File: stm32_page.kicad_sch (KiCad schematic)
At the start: 20 parts, among them J1 FTSH-107-01-L-DV-K-A, U1 STM32L431KBU6_C2826408, X1 SC-32S32.768kHz20PPM7pF

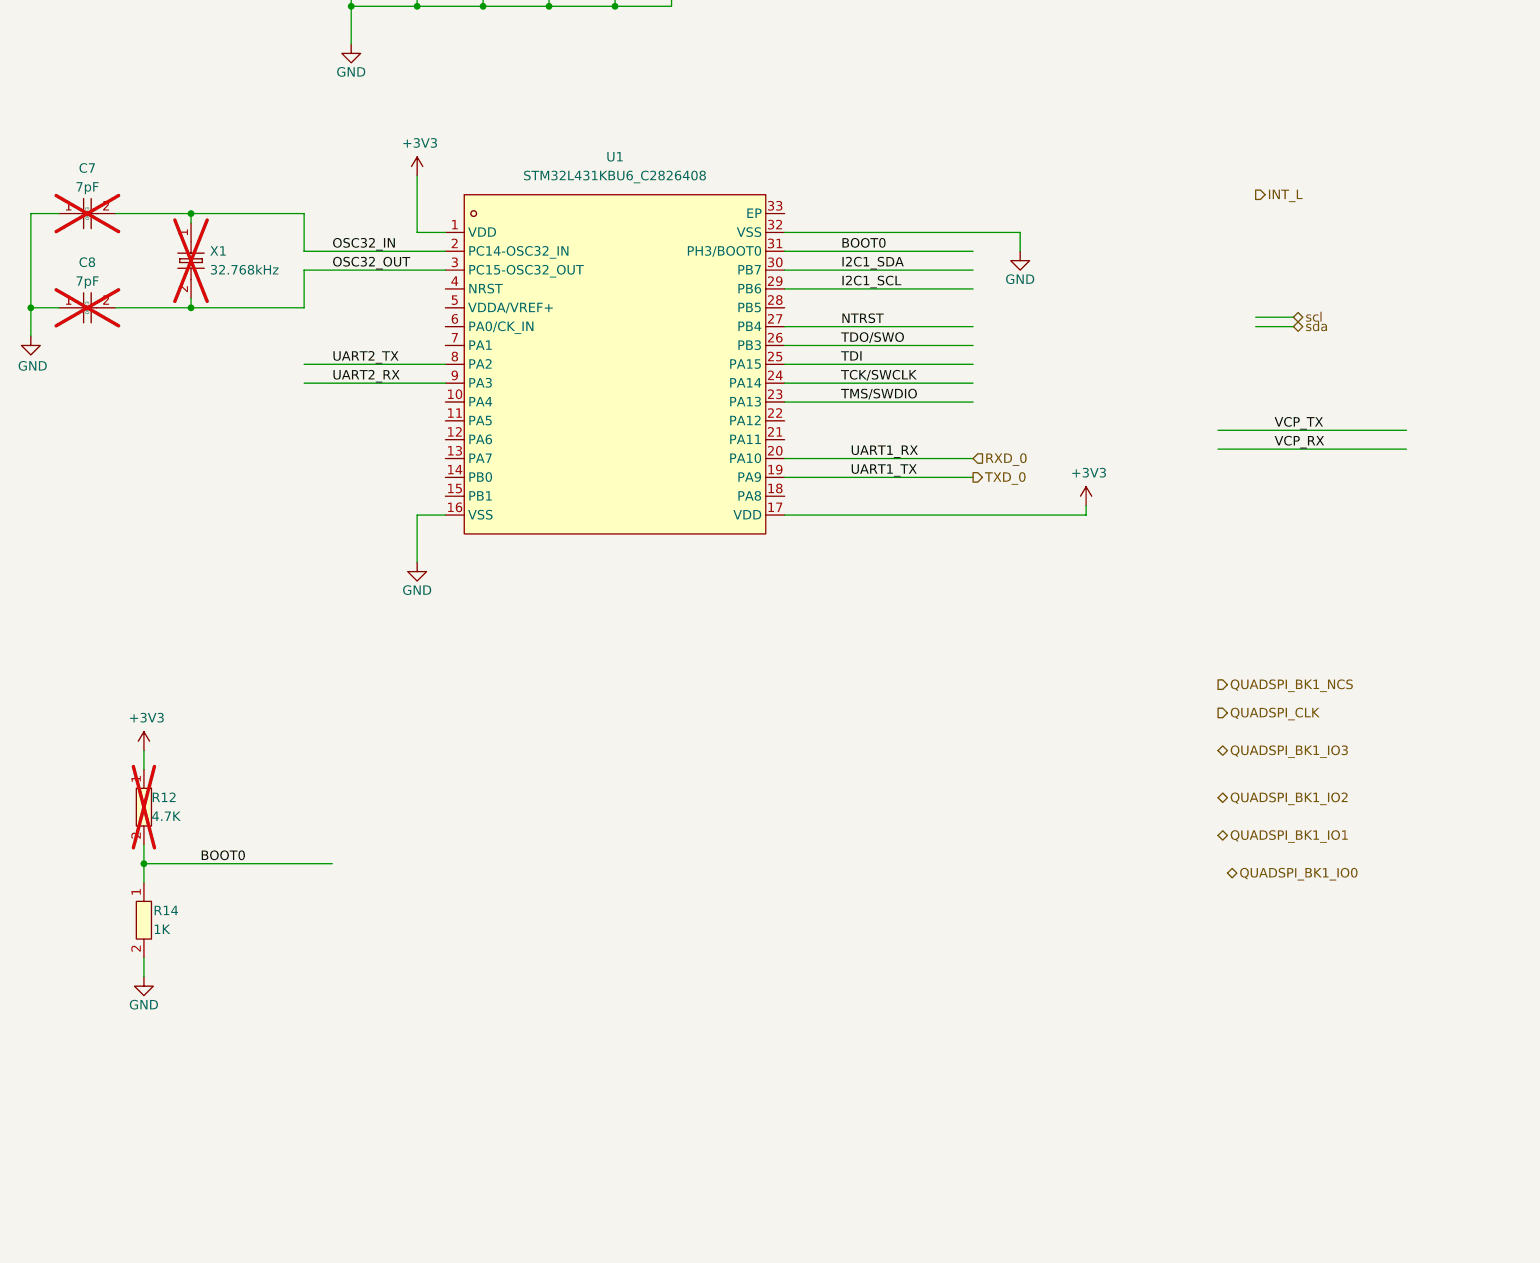
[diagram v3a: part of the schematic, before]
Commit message: Add IO pinout - 2 I2C, 2UART, 1 SPI, LEDs, switches,2 interupts,RST
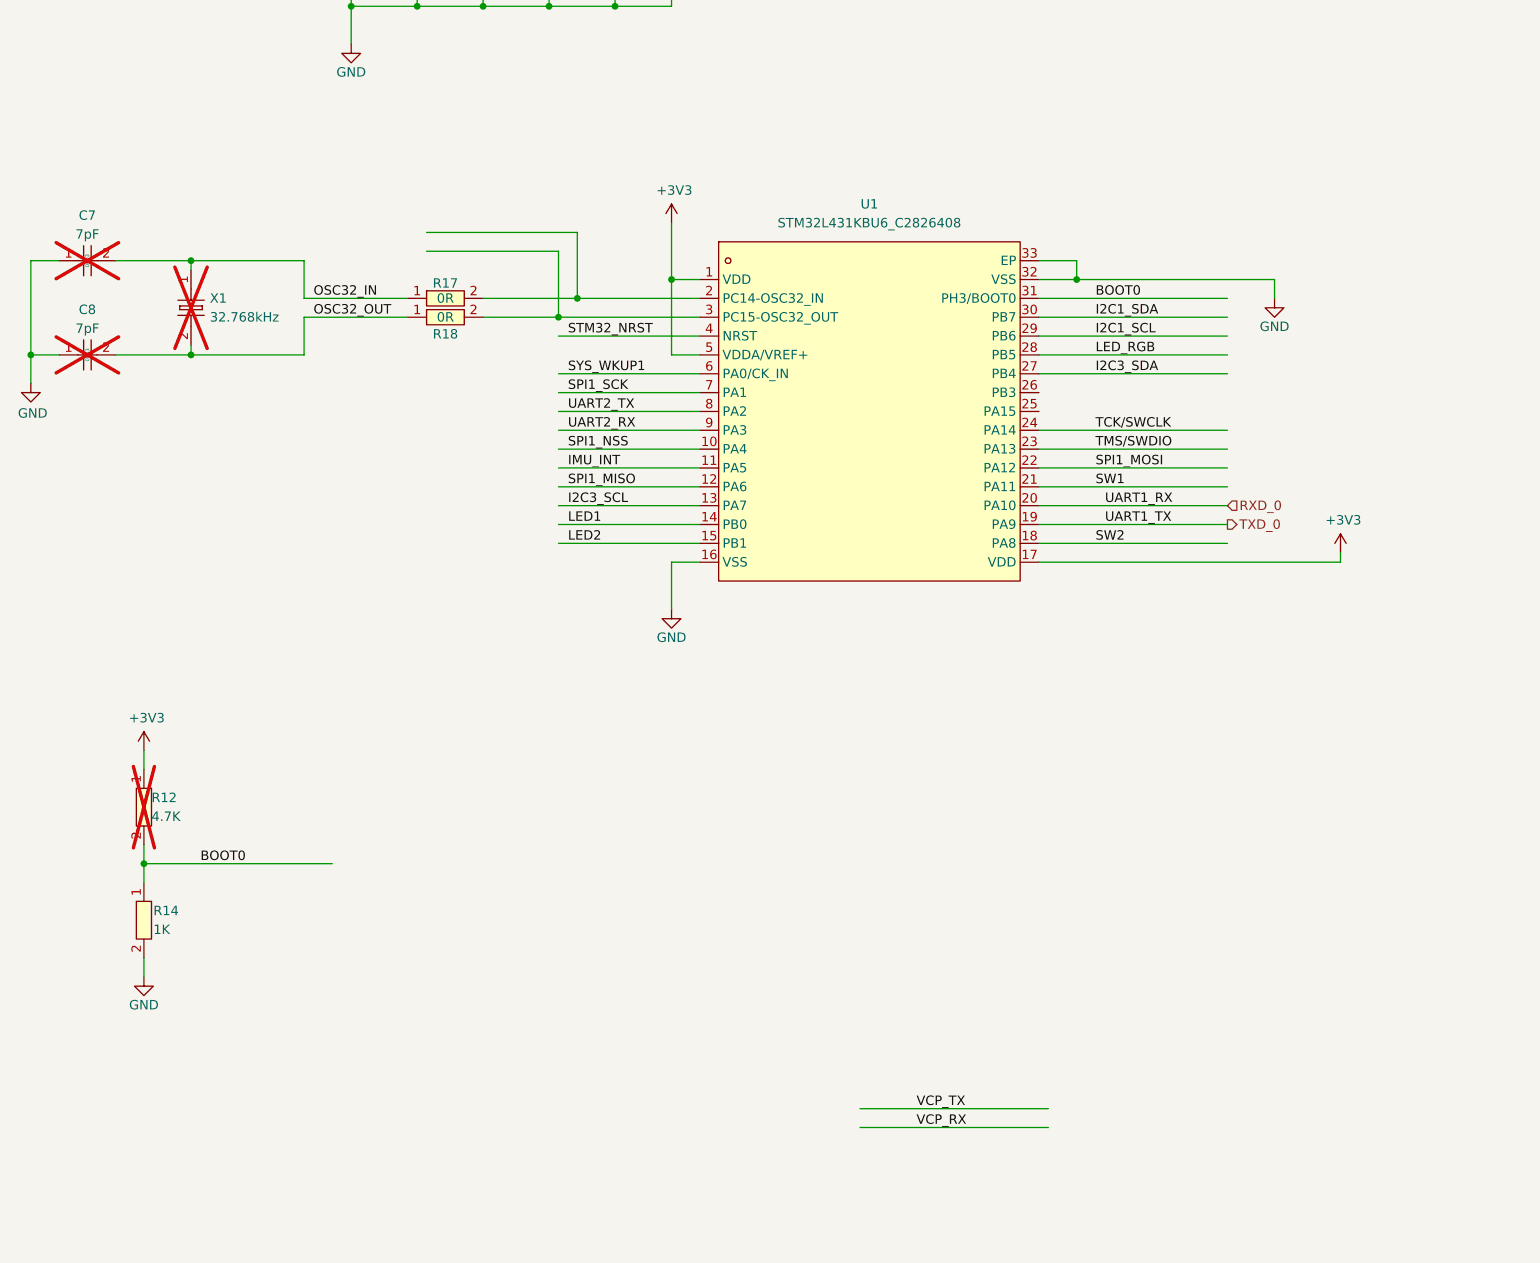
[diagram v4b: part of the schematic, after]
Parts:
- added R17, R18: 0603WAF0000T5E, easyeda2kicad:R0603, symbol easyeda2kicad:0603WAF0000T5E
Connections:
- net +3V3: now also U1.5 (VDDA/VREF+)
- net GND: now also U1.33 (EP)
- net NTRST: no longer U1.27 (PB4)
- net OSC32_IN: now also R17.1; no longer U1.2 (PC14-OSC32_IN)
- net OSC32_OUT: now also R18.1; no longer U1.3 (PC15-OSC32_OUT)
- net TDI: no longer U1.25 (PA15)
- net TDO/SWO: no longer U1.26 (PB3)
- net SPI1_NSS: now reaches U1.10 (PA4)
- net IMU_INT: now reaches U1.11 (PA5)
- net SPI1_MISO: now reaches U1.12 (PA6)
- net I2C3_SCL: now reaches U1.13 (PA7)
- net LED1: now reaches U1.14 (PB0)
- net LED2: now reaches U1.15 (PB1)
- net SW2: now reaches U1.18 (PA8)
- net SW1: now reaches U1.21 (PA11)
- net SPI1_MOSI: now reaches U1.22 (PA12)
- net LED_RGB: now reaches U1.28 (PB5)
- net STM32_NRST: now reaches U1.4 (NRST)
- net SYS_WKUP1: now reaches U1.6 (PA0/CK_IN)
- net SPI1_SCK: now reaches U1.7 (PA1)
- new net: R17.2, U1.2 (PC14-OSC32_IN)
- new net: R18.2, U1.3 (PC15-OSC32_OUT)
- new net I2C3_SDA: U1.27 (PB4)
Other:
- moved on the sheet: C7, C8, U1, X1

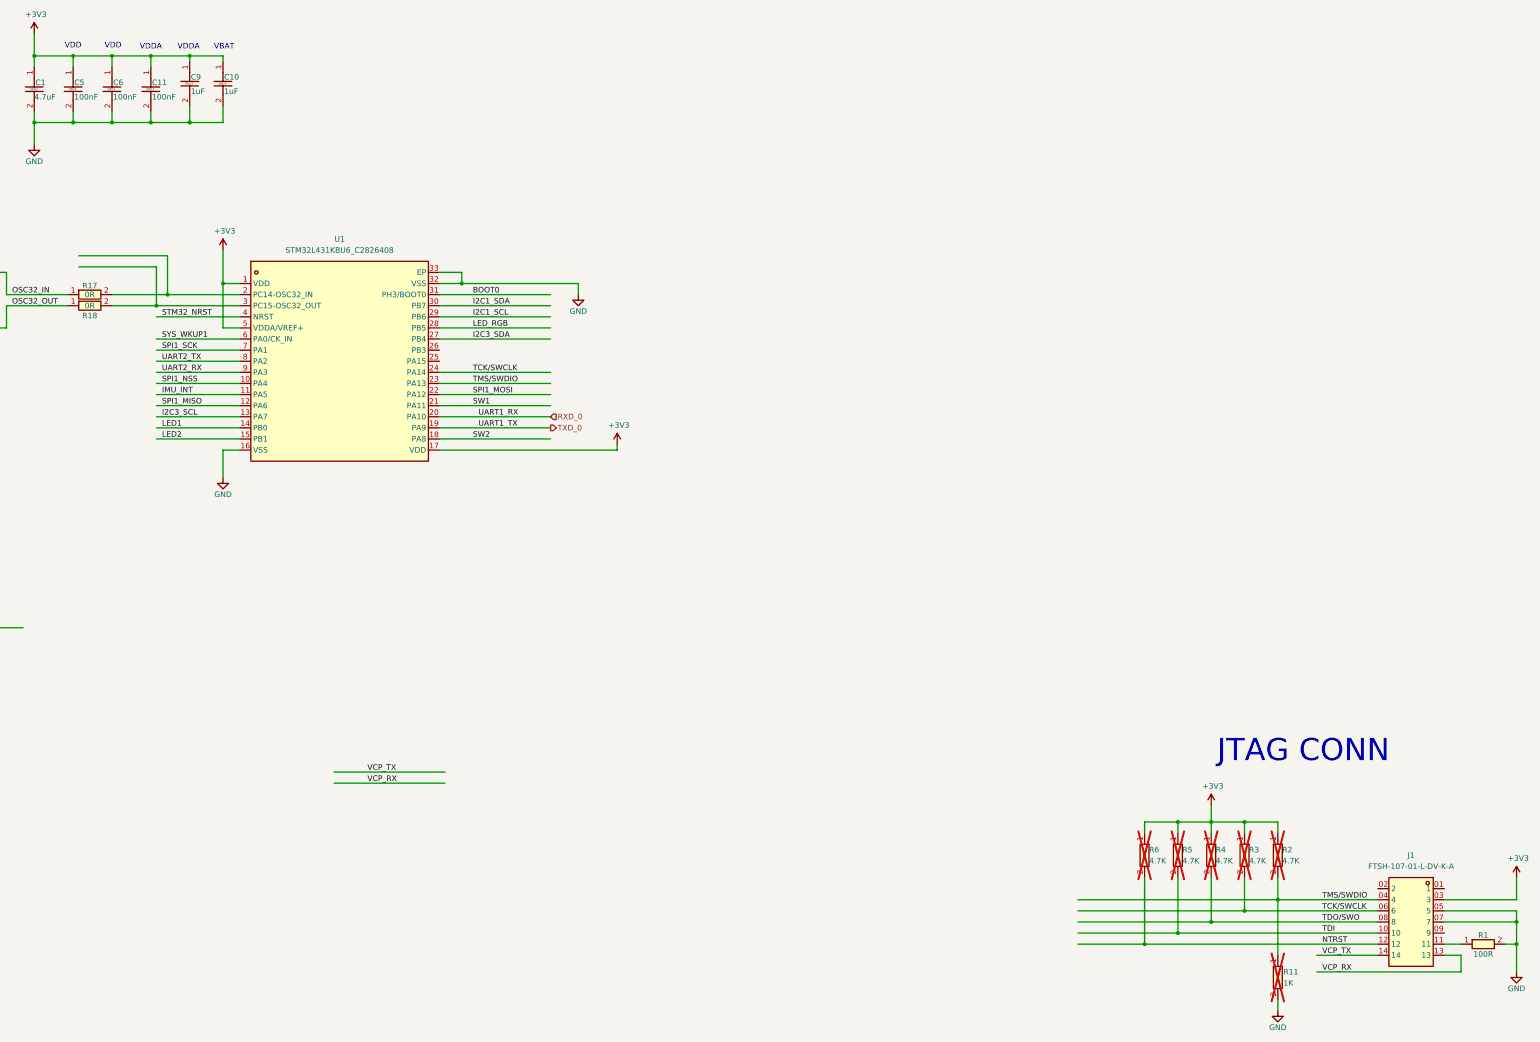
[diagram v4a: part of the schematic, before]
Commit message: Add LEDs,22r to I2C, UART conv, power conn, remove JTAG to SW debug
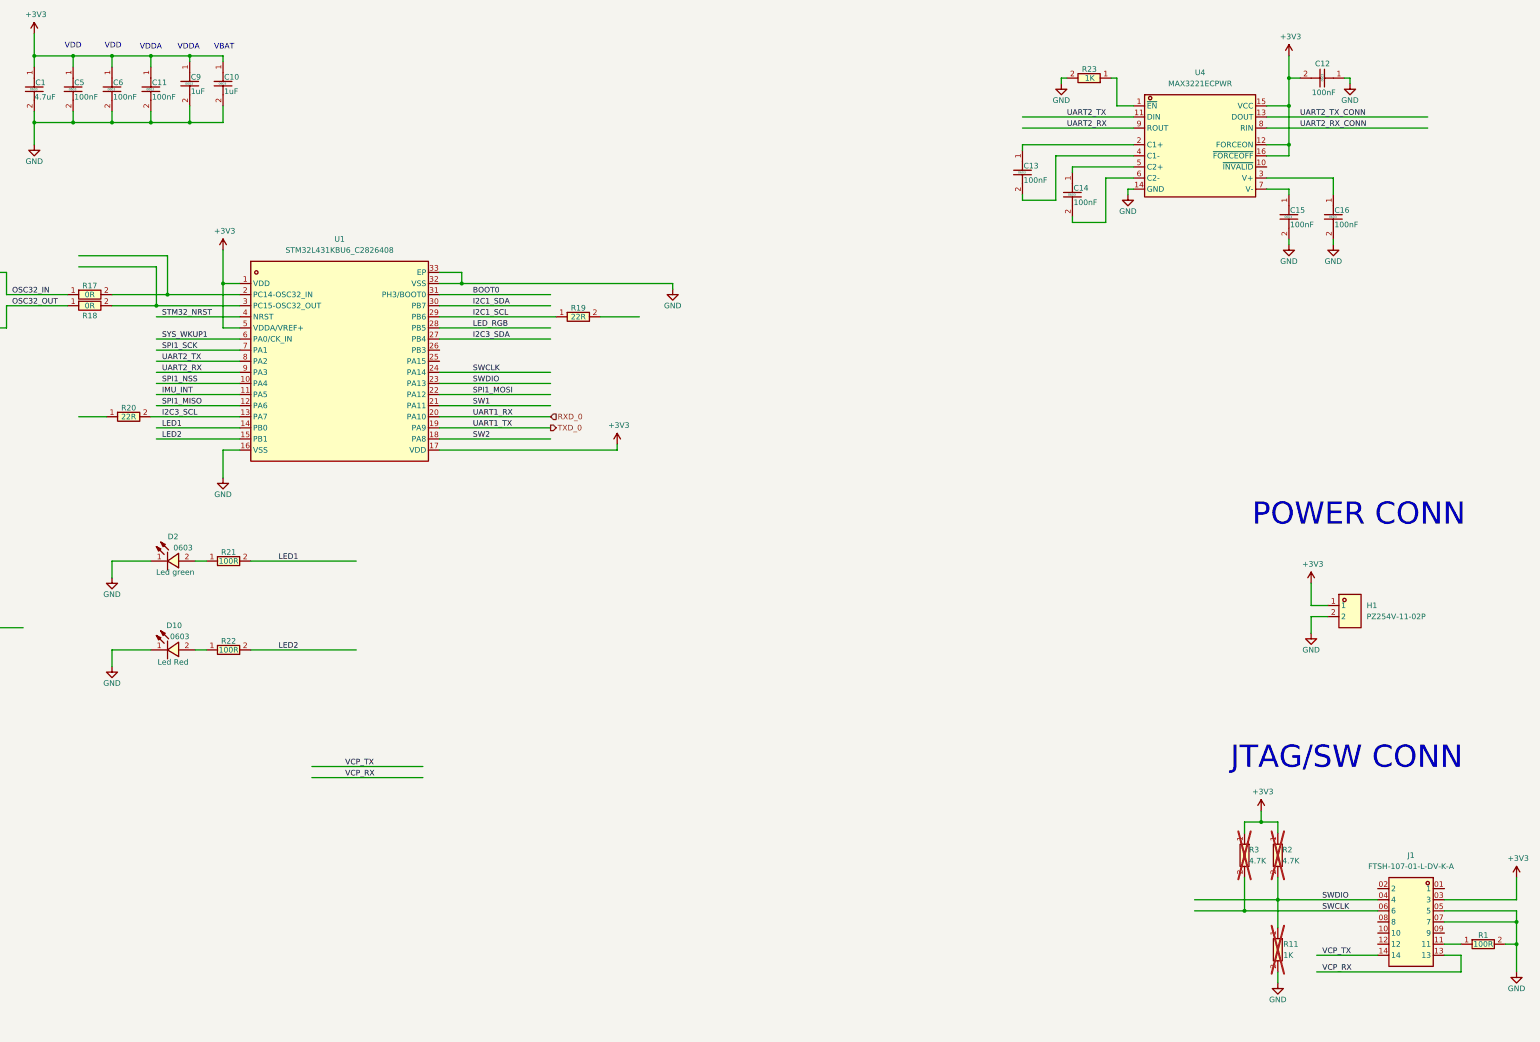
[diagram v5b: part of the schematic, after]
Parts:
- removed R4, R5, R6: 0603WAF4701T5E, easyeda2kicad:R0603, symbol easyeda2kicad:0603WAF4701T5E
- added C12, C13, C14, C15, C16: CC0603KRX7R9BB104, easyeda2kicad:C0603, symbol easyeda2kicad:CC0603KRX7R9BB104
- added D10: KT-0603R, easyeda2kicad:LED0603-RD, symbol easyeda2kicad:KT-0603R
- added D2: 0603 Green 509-620mcd, easyeda2kicad:LED0603-RD, symbol easyeda2kicad:0603Green509-620mcd
- added H1: PZ254V-11-02P, easyeda2kicad:HDR-TH_2P-P2.54-V-M, symbol easyeda2kicad:PZ254V-11-02P
- added R19, R20: 0603WAF220JT5E, easyeda2kicad:R0603, symbol easyeda2kicad:0603WAF220JT5E
- added R21, R22: 0603WAF1000T5E, easyeda2kicad:R0603, symbol easyeda2kicad:0603WAF1000T5E
- added R23: 0603WAF1001T5E, easyeda2kicad:R0603, symbol easyeda2kicad:0603WAF1001T5E
- added U4: MAX3221ECPWR, easyeda2kicad:TSSOP-16_L5.0-W4.4-P0.65-LS6.4-BL, symbol easyeda2kicad:MAX3221ECPWR
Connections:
- net +3V3: now also C12.2, H1.1, U4.12 (FORCEON), U4.15 (VCC), U4.16 (~{FORCEOFF})
- net GND: now also C12.1, C15.2, C16.2, D10.1 (K), D2.1 (K), H1.2, R23.2, U4.14 (GND)
- net I2C1_SCL: now also R19.1
- net I2C3_SCL: now also R20.2
- net LED1: now also R21.2
- net LED2: now also R22.2
- net UART2_RX: now also U4.9 (ROUT)
- net UART2_TX: now also U4.11 (DIN)
- net NTRST: no longer names the net of J1.12
- net TCK/SWCLK renamed SWCLK
- net TDI: no longer names the net of J1.10
- net TDO/SWO: no longer names the net of J1.08 (8)
- net TMS/SWDIO renamed SWDIO
- new net: C15.1, U4.7 (V-)
- new net: R23.1, U4.1 (~{EN})
- new net: C13.1, U4.2 (C1+)
- new net: C13.2, U4.4 (C1-)
- new net: D2.2 (A), R21.1
- new net: C14.1, U4.5 (C2+)
- new net: C14.2, U4.6 (C2-)
- new net: C16.1, U4.3 (V+)
- new net: D10.2 (A), R22.1
- new net UART2_RX_CONN: U4.8 (RIN)
- new net UART2_TX_CONN: U4.13 (DOUT)
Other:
- note added: "JTAG/SW CONN"
- note added: "POWER CONN"
- note removed: "JTAG CONN"
- moved on the sheet: R11

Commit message: add SD_CD, PB_SW for NRST, 22R for RGB, 1X3 headers for uart and VCP option, block ports
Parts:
- removed H1: PZ254V-11-02P, easyeda2kicad:HDR-TH_2P-P2.54-V-M, symbol easyeda2kicad:PZ254V-11-02P
- added J2, J4, J5: PZ254V-11-03P_C2937625, easyeda2kicad:HDR-TH_3P-P2.54-V-M, symbol easyeda2kicad:PZ254V-11-03P_C2937625
- added R24, R25: 0603WAF4701T5E, easyeda2kicad:R0603, symbol easyeda2kicad:0603WAF4701T5E
- added R26, R27: 0603WAF0000T5E, easyeda2kicad:R0603, symbol easyeda2kicad:0603WAF0000T5E
- added R28: 0603WAF220JT5E, easyeda2kicad:R0603, symbol easyeda2kicad:0603WAF220JT5E
- added SW2, SW3: 6.0*6.0*6.0, easyeda2kicad:SW-SMD_4P-L6.0-W6.0-P4.50-LS8.6, symbol easyeda2kicad:6.0*6.0*6.0
- R17, R18: now not fitted; now left out of the parts list
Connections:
- net +3V3: now also R24.1, R25.1
- net GND: now also J2.3, SW2.3, SW2.4, SW3.3, SW3.4
- net I2C1_SCL: now also R19.2; no longer R19.1, U1.29 (PB6)
- net I2C3_SCL: now also R20.1; no longer R20.2, U1.13 (PA7)
- net STM32_NRST: now also R25.2, SW3.1, SW3.2
- net UART2_RX: now also J5.2; no longer U4.9 (ROUT)
- net UART2_RX_CONN: now also J2.2
- net UART2_TX: now also J4.2; no longer U4.11 (DIN)
- net UART2_TX_CONN: now also J2.1
- net VCP_RX: now also J5.3
- net VCP_TX: now also J4.3
- net at R17.2, U1.2 (PC14-OSC32_IN): now also R26.2
- net at R18.2, U1.3 (PC15-OSC32_OUT): now also R27.2
- net LED_RGB renamed RGB_LEDS_R
- net RGB_LEDS_R: now also R28.1, R28.2
- net RXD_0 renamed UART1_RX
- net SPI1_NSS renamed SD_CD
- net SW1 renamed PB_SW1
- net PB_SW1: now also R24.2, SW2.1, SW2.2
- net SW2: no longer names the net of U1.18 (PA8)
- net TXD_0 renamed UART1_TX
- new net I2C1_SCL_R: R19.1, U1.29 (PB6)
- new net I2C3_SCL_R: R20.2, U1.13 (PA7)
- new net MAX3221_RX_OUT: J5.1, U4.9 (ROUT)
- new net MAX3221_TX_IN: J4.1, U4.11 (DIN)
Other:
- note added: "UART2"
- note removed: "POWER CONN"
- moved on the sheet: C1, C10, C11, C12, C13, C14, C15, C16, C5, C6, C7, C8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
